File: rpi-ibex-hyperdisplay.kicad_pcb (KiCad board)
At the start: 2 copper layers, 99.1 x 113.5 mm, 66 parts, among them J1 Conn_02x05_Odd_Even, J2 USART_Connector_1, J3 Raspberry_Pi_2_3, J4 Hyperpixel_4.0_Touch, U1 ATmega328PB-AU, Y1 16MHz

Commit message: mirror flip the hyperpixel connector (oops :/)
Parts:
- 2/@ ('): renamed from 2/@ (`)
- 7/& (`): renamed from 7/& (')
- moved J3 12.5 mm to (135.6, 68.3), turned to 180 degrees
- moved J4 3.59 mm to (132.3, 66.8)
- renumbered 10K to R1, 1K to R2, 1K to R3
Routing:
- net BCM1: track 17.6 -> 160.1 mm, vias 0 -> 1
- net BCM0: track 11.4 -> 146.1 mm, vias 0 -> 1
- net BCM7: track 17.6 -> 147.9 mm, vias 0 -> 1
- net RPI_3.3V: track 213.0 -> 340.9 mm, vias 8 -> 12
- net BCM8: track 17.6 -> 139.2 mm, vias 0 -> 1
- net BCM25: track 17.6 -> 126.0 mm, vias 0 -> 1
- net BCM11: track 83.1 -> 187.2 mm, vias 2 -> 4
- net BCM9: track 11.4 -> 105.4 mm, vias 0 -> 1
- net BCM24: track 17.6 -> 105.6 mm, vias 0 -> 1
- net BCM23: track 17.6 -> 98.0 mm, vias 0 -> 1
- net BCM22: track 11.4 -> 91.5 mm, vias 0 -> 1
- net BCM10: track 82.1 -> 160.0 mm, vias 2 -> 4
- net BCM18: track 17.6 -> 91.4 mm, vias 0 -> 1
- net BCM27: track 11.4 -> 84.9 mm, vias 0 -> 1
- net BCM17: track 11.4 -> 81.0 mm, vias 0 -> 1
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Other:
- board text added: "Yovan Naumovski, 2019 rpi-ibex v0.4"
- board text removed: "Yovan Naumovski, 2019 rpi-ibex v0.3"

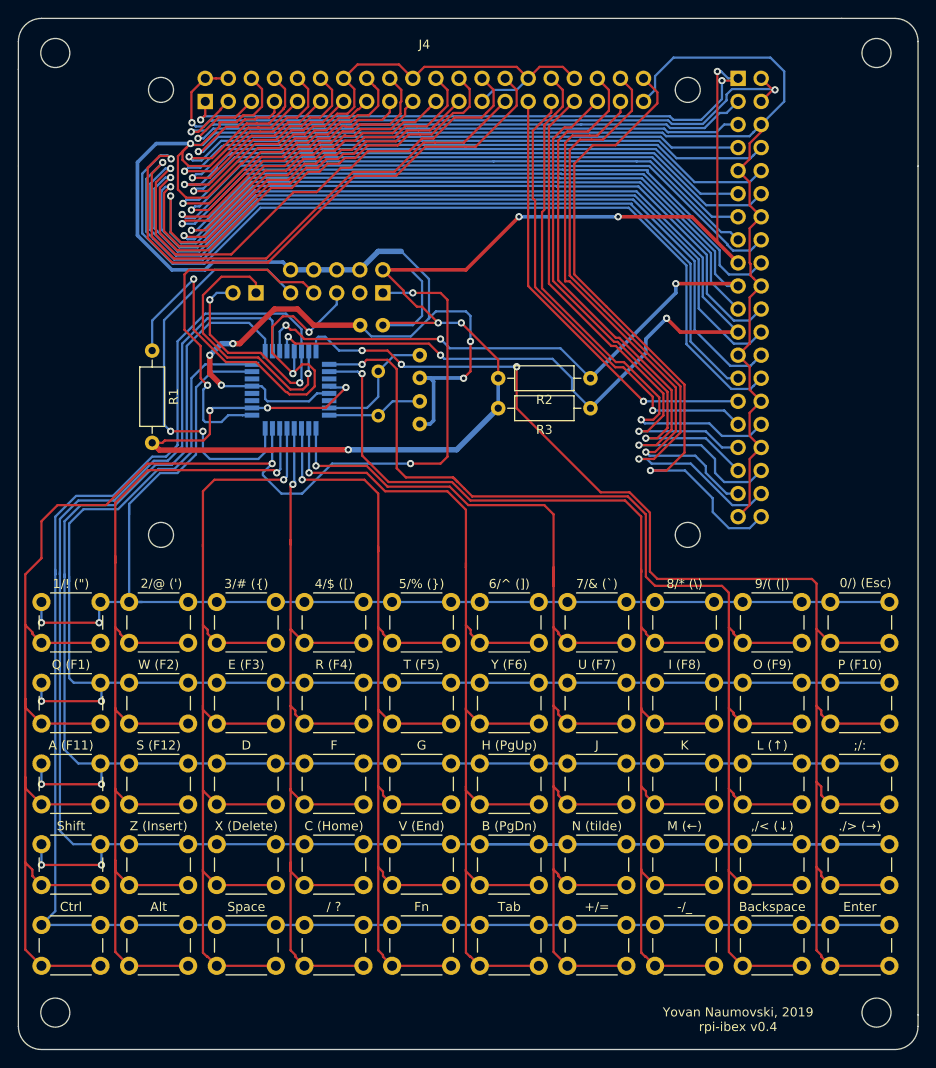
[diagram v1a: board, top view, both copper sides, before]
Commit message: move hyperpixel footprint silkscreen and other layers from back to front
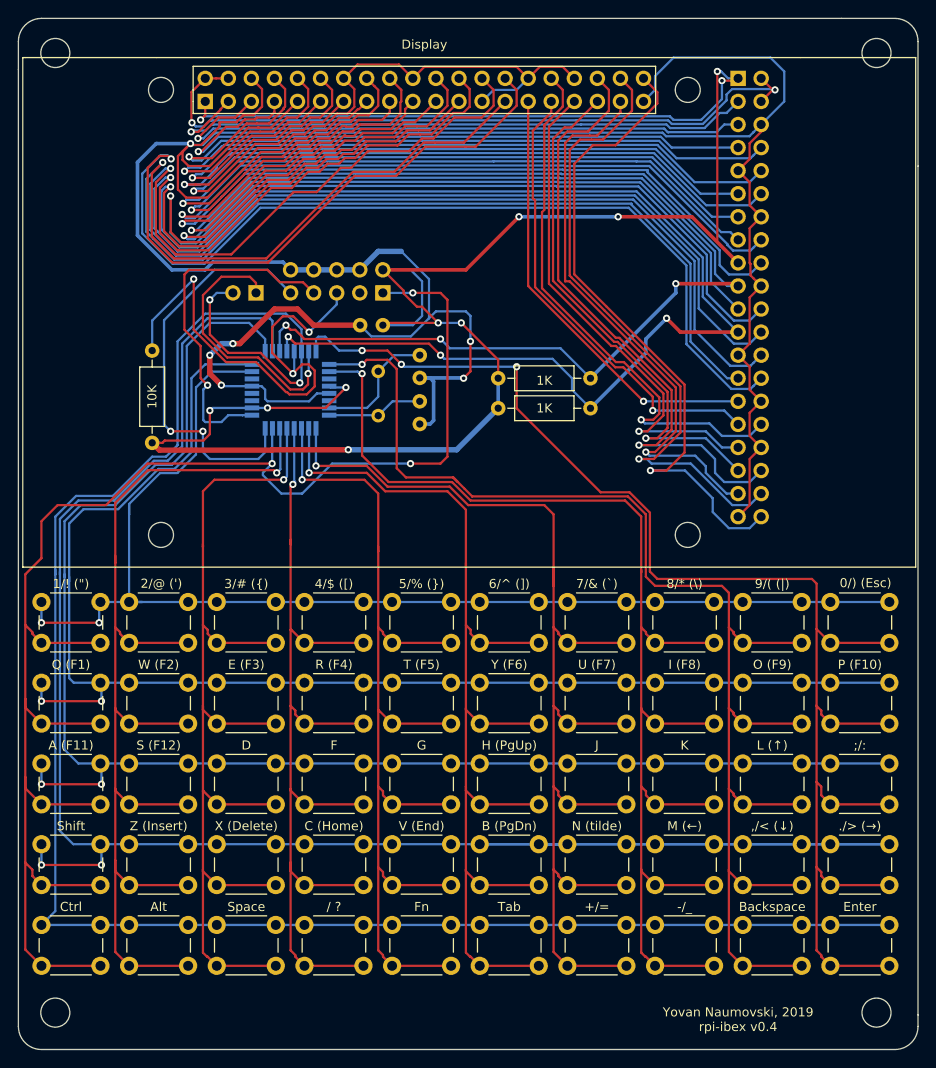
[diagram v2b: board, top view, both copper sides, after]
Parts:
- removed J4: Hyperpixel_4.0_Touch, TFT_modules:Hyperpixel_4.0_Touch
- added Display: Hyperpixel_4.0_Touch, TFT_modules:Hyperpixel_4.0_Touch, F.Cu at (132.3, 66.8)
- renumbered R1 to 10K, R2 to 1K, R3 to 1K
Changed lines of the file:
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@@
   (page A4)
   (layers
-    (0 F.Cu signal)
-    (31 B.Cu signal)
+    (0 F.Cu signal hide)
+    (31 B.Cu signal hide)
     (32 B.Adhes user)
-    (33 F.Adhes user)
+    (33 F.Adhes user hide)
     (34 B.Paste user)
     (35 F.Paste user)
@@
     (descr "Resistor, Axial_DIN0207 series, Axial, Horizontal, pin pitch=10.16mm, 0.25W = 1/4W, length*diameter=6.3*2.5mm^2, http://cdn-reichelt.de/documents/datenblatt/B400/1_4W%23YAG.pdf")
     (tags "Resistor Axial_DIN0207 series Axial Horizontal pin pitch 10.16mm 0.25W = 1/4W length 6.3mm diameter 2.5mm")
-    (fp_text reference R2 (at 5.08 -2.37) (layer F.SilkS)
+    (fp_text reference 1K (at 5.08 -0.254) (layer F.SilkS)
       (effects (font (size 1 1) (thickness 0.15)))
     )
@@
     (descr "Resistor, Axial_DIN0207 series, Axial, Horizontal, pin pitch=10.16mm, 0.25W = 1/4W, length*diameter=6.3*2.5mm^2, http://cdn-reichelt.de/documents/datenblatt/B400/1_4W%23YAG.pdf")
     (tags "Resistor Axial_DIN0207 series Axial Horizontal pin pitch 10.16mm 0.25W = 1/4W length 6.3mm diameter 2.5mm")
-    (fp_text reference R1 (at 5.08 -2.37 90) (layer F.SilkS)
+    (fp_text reference 10K (at 5.08 0 90) (layer F.SilkS)
       (effects (font (size 1 1) (thickness 0.15)))
     )
@@
     (descr "Resistor, Axial_DIN0207 series, Axial, Horizontal, pin pitch=10.16mm, 0.25W = 1/4W, length*diameter=6.3*2.5mm^2, http://cdn-reichelt.de/documents/datenblatt/B400/1_4W%23YAG.pdf")
     (tags "Resistor Axial_DIN0207 series Axial Horizontal pin pitch 10.16mm 0.25W = 1/4W length 6.3mm diameter 2.5mm")
-    (fp_text reference R3 (at 5.08 -2.37) (layer F.SilkS)
+    (fp_text reference 1K (at 5.08 0) (layer F.SilkS)
       (effects (font (size 1 1) (thickness 0.15)))
     )
@@
     (descr "Raspberry Pi Zero using through hole straight pin socket, 2x20, 2.54mm pitch, https://www.raspberrypi.org/documentation/hardware/raspberrypi/mechanical/rpi_MECH_Zero_1p2.pdf")
     (tags "raspberry pi zero through hole")
-    (fp_text reference J4 (at -2.206 31.242) (layer F.SilkS)
+    (fp_text reference Display (at -2.206 31.242) (layer F.SilkS)
       (effects (font (size 1 1) (thickness 0.15)))
     )
-    (fp_text value Hyperpixel_4.0_Touch (at 14.294 31.242) (layer B.Fab)
-      (effects (font (size 1 1) (thickness 0.15)) (justify mirror))
+    (fp_text value Hyperpixel_4.0_Touch (at 14.294 31.242) (layer F.Fab)
+      (effects (font (size 1 1) (thickness 0.15)))
     )
-    (fp_line (start -0.766 1.742) (end -0.766 60.742) (layer B.SilkS) (width 0.12))
-    (fp_line (start 5.334 55.642) (end 5.334 5.842) (layer B.Fab) (width 0.1))
-    (fp_line (start 0.254 56.642) (end 4.334 56.642) (layer B.Fab) (width 0.1))
-    (fp_line (start 4.334 56.642) (end 5.334 55.642) (layer B.Fab) (width 0.1))
-    (fp_line (start 0.194 5.782) (end 5.394 5.782) (layer B.SilkS) (width 0.12))
-    (fp_line (start 5.394 54.102) (end 5.394 5.782) (layer B.SilkS) (width 0.12))
-    (fp_line (start 5.394 56.702) (end 5.394 55.372) (layer B.SilkS) (width 0.12))
-    (fp_line (start 4.064 56.702) (end 5.394 56.702) (layer B.SilkS) (width 0.12))
-    (fp_line (start 2.794 54.102) (end 5.394 54.102) (layer B.SilkS) (width 0.12))
-    (fp_line (start 2.794 56.702) (end 2.794 54.102) (layer B.SilkS) (width 0.12))
-    (fp_line (start 5.824 5.372) (end -0.276 5.372) (layer B.CrtYd) (width 0.05))
-    (fp_line (start -0.276 5.372) (end -0.276 57.172) (layer B.CrtYd) (width 0.05))
-    (fp_line (start -0.276 57.172) (end 5.824 57.172) (layer B.CrtYd) (width 0.05))
-    (fp_line (start 5.824 57.172) (end 5.824 5.372) (layer B.CrtYd) (width 0.05))
-    (fp_line (start 0.194 56.702) (end 2.794 56.702) (layer B.SilkS) (width 0.12))
-    (fp_line (start 0.194 56.702) (end 0.194 5.782) (layer B.SilkS) (width 0.12))
-    (fp_line (start 5.334 5.842) (end 0.254 5.842) (layer B.Fab) (width 0.1))
-    (fp_line (start 0.254 5.842) (end 0.254 56.642) (layer B.Fab) (width 0.1))
-    (fp_text user %R (at 2.794 31.242 180) (layer B.Fab)
-      (effects (font (size 1 1) (thickness 0.15)) (justify mirror))
-    )
-    (fp_line (start -0.706 1.742) (end -0.706 60.742) (layer B.Fab) (width 0.1))
-    (fp_line (start -0.766 60.742) (end -0.766 68.616) (layer B.SilkS) (width 0.12))
-    (fp_line (start -0.766 68.616) (end -0.766 75.184) (layer B.SilkS) (width 0.12))
-    (fp_line (start -0.766 75.184) (end -0.766 75.438) (layer B.SilkS) (width 0.12))
-    (fp_line (start -0.766 1.742) (end -0.766 -10.196) (layer B.SilkS) (width 0.12))
-    (fp_line (start -0.766 -10.196) (end -0.766 -22.86) (layer B.SilkS) (width 0.12))
-    (fp_line (start -0.706 60.742) (end -0.706 75.22) (layer B.Fab) (width 0.12))
-    (fp_line (start -0.706 75.22) (end -0.706 75.4232) (layer B.Fab) (width 0.12))
-    (fp_line (start 55.3264 60.1578) (end 55.3264 71.537) (layer B.Fab) (width 0.12))
-    (fp_line (start -0.706 75.4232) (end 55.0978 75.4232) (layer B.Fab) (width 0.12))
-    (fp_line (start 55.3264 71.537) (end 55.3264 75.3978) (layer B.Fab) (width 0.12))
-    (fp_line (start 55.0978 75.4232) (end 55.301 75.4232) (layer B.Fab) (width 0.12))
-    (fp_line (start 55.301 75.4232) (end 55.3264 75.4232) (layer B.Fab) (width 0.12))
-    (fp_line (start -0.706 1.742) (end -0.706 -22.8494) (layer B.Fab) (width 0.12))
-    (fp_line (start -0.706 -22.8494) (end 54.2342 -22.8494) (layer B.Fab) (width 0.12))
-    (fp_line (start 55.3264 60.1578) (end 55.3264 -22.8494) (layer B.Fab) (width 0.12))
-    (fp_line (start 54.2342 -22.8494) (end 55.3264 -22.8494) (layer B.Fab) (width 0.12))
-    (fp_line (start -0.766 -22.86) (end 55.3426 -22.86) (layer B.SilkS) (width 0.12))
-    (fp_line (start 55.3426 -22.86) (end 55.3426 75.4634) (layer B.SilkS) (width 0.12))
-    (fp_line (start 55.3426 75.4634) (end -0.766 75.4634) (layer B.SilkS) (width 0.12))
+    (fp_line (start -0.766 1.742) (end -0.766 60.742) (layer F.SilkS) (width 0.12))
+    (fp_line (start 5.334 55.642) (end 5.334 5.842) (layer F.Fab) (width 0.1))
+    (fp_line (start 0.254 56.642) (end 4.334 56.642) (layer F.Fab) (width 0.1))
+    (fp_line (start 5.334 56.642) (end 5.334 55.642) (layer F.Fab) (width 0.1))
+    (fp_line (start 0.194 5.782) (end 5.394 5.782) (layer F.SilkS) (width 0.12))
+    (fp_line (start 5.394 54.102) (end 5.394 5.782) (layer F.SilkS) (width 0.12))
+    (fp_line (start 5.394 56.702) (end 5.394 55.372) (layer F.SilkS) (width 0.12))
+    (fp_line (start 4.064 56.702) (end 5.394 56.702) (layer F.SilkS) (width 0.12))
+    (fp_line (start 5.394 55.372) (end 5.394 54.102) (layer F.SilkS) (width 0.12))
+    (fp_line (start 2.794 56.702) (end 4.064 56.702) (layer F.SilkS) (width 0.12))
+    (fp_line (start 5.824 5.372) (end -0.276 5.372) (layer F.CrtYd) (width 0.05))
+    (fp_line (start -0.276 5.372) (end -0.276 57.172) (layer F.CrtYd) (width 0.05))
+    (fp_line (start -0.276 57.172) (end 5.824 57.172) (layer F.CrtYd) (width 0.05))
+    (fp_line (start 5.824 57.172) (end 5.824 5.372) (layer F.CrtYd) (width 0.05))
+    (fp_line (start 0.194 56.702) (end 2.794 56.702) (layer F.SilkS) (width 0.12))
+    (fp_line (start 0.194 56.702) (end 0.194 5.782) (layer F.SilkS) (width 0.12))
+    (fp_line (start 5.334 5.842) (end 0.254 5.842) (layer F.Fab) (width 0.1))
+    (fp_line (start 0.254 5.842) (end 0.254 56.642) (layer F.Fab) (width 0.1))
+    (fp_text user %R (at 2.794 31.242 180) (layer F.Fab)
+      (effects (font (size 1 1) (thickness 0.15)) (justify mirror))
+    )
+    (fp_line (start -0.706 1.742) (end -0.706 60.742) (layer F.Fab) (width 0.1))
+    (fp_line (start -0.766 60.742) (end -0.766 68.616) (layer F.SilkS) (width 0.12))
+    (fp_line (start -0.766 68.616) (end -0.766 75.184) (layer F.SilkS) (width 0.12))
+    (fp_line (start -0.766 75.184) (end -0.766 75.438) (layer F.SilkS) (width 0.12))
+    (fp_line (start -0.766 1.742) (end -0.766 -10.196) (layer F.SilkS) (width 0.12))
+    (fp_line (start -0.766 -10.196) (end -0.766 -22.86) (layer F.SilkS) (width 0.12))
+    (fp_line (start -0.706 60.742) (end -0.706 75.22) (layer F.Fab) (width 0.12))
+    (fp_line (start -0.706 75.22) (end -0.706 75.4232) (layer F.Fab) (width 0.12))
+    (fp_line (start 55.3264 60.1578) (end 55.3264 71.537) (layer F.Fab) (width 0.12))
+    (fp_line (start -0.706 75.4232) (end 55.0978 75.4232) (layer F.Fab) (width 0.12))
+    (fp_line (start 55.3264 71.537) (end 55.3264 75.3978) (layer F.Fab) (width 0.12))
+    (fp_line (start 55.0978 75.4232) (end 55.301 75.4232) (layer F.Fab) (width 0.12))
+    (fp_line (start 55.301 75.4232) (end 55.3264 75.4232) (layer F.Fab) (width 0.12))
+    (fp_line (start -0.706 1.742) (end -0.706 -22.8494) (layer F.Fab) (width 0.12))
+    (fp_line (start -0.706 -22.8494) (end 54.2342 -22.8494) (layer F.Fab) (width 0.12))
+    (fp_line (start 55.3264 60.1578) (end 55.3264 -22.8494) (layer F.Fab) (width 0.12))
+    (fp_line (start 54.2342 -22.8494) (end 55.3264 -22.8494) (layer F.Fab) (width 0.12))
+    (fp_line (start -0.766 -22.86) (end 55.3426 -22.86) (layer F.SilkS) (width 0.12))
+    (fp_line (start 55.3426 -22.86) (end 55.3426 75.4634) (layer F.SilkS) (width 0.12))
+    (fp_line (start 55.3426 75.4634) (end -0.766 75.4634) (layer F.SilkS) (width 0.12))
     (fp_line (start -0.766 75.4634) (end -0.766 75.438) (layer B.SilkS) (width 0.12))
+    (fp_line (start 4.334 56.642) (end 5.334 56.642) (layer F.Fab) (width 0.1))
     (pad 6 thru_hole oval (at 1.524 50.292 270) (size 1.7 1.7) (drill 1) (layers *.Cu *.Mask)
       (net 1 GND))

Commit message: rotate the rpi pin headers so that its usb ports are facing outwards the board
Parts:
- moved J3 50.1 mm to (137.9, 118.4), turned to 0 degrees
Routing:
- net RPI_3.3V: track 340.9 -> 562.1 mm, vias 12 -> 13
- net BCM5: track 48.7 -> 166.8 mm, vias 1 -> 2
- net BCM10: track 160.0 -> 241.8 mm
- net BCM11: track 187.2 -> 264.4 mm
- net BCM21: track 72.9 -> 14.1 mm, vias 1 -> 0
- net GND: track 369.5 -> 427.8 mm, vias 6 -> 12
- net BCM20: track 70.8 -> 21.3 mm, vias 1 -> 2
- net BCM16: track 69.1 -> 21.7 mm, vias 1 -> 0
- net BCM3: track 68.0 -> 112.8 mm, vias 1 -> 2
- net BCM2: track 67.5 -> 110.4 mm, vias 1 -> 2
- net BCM4: track 72.0 -> 112.5 mm, vias 1 -> 2
- net BCM26: track 62.5 -> 22.6 mm, vias 1 -> 0
- net BCM12: track 61.0 -> 26.6 mm, vias 1 -> 0
- net BCM17: track 81.0 -> 114.2 mm, vias 1 -> 2
- net BCM13: track 56.3 -> 23.2 mm, vias 1 -> 0
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
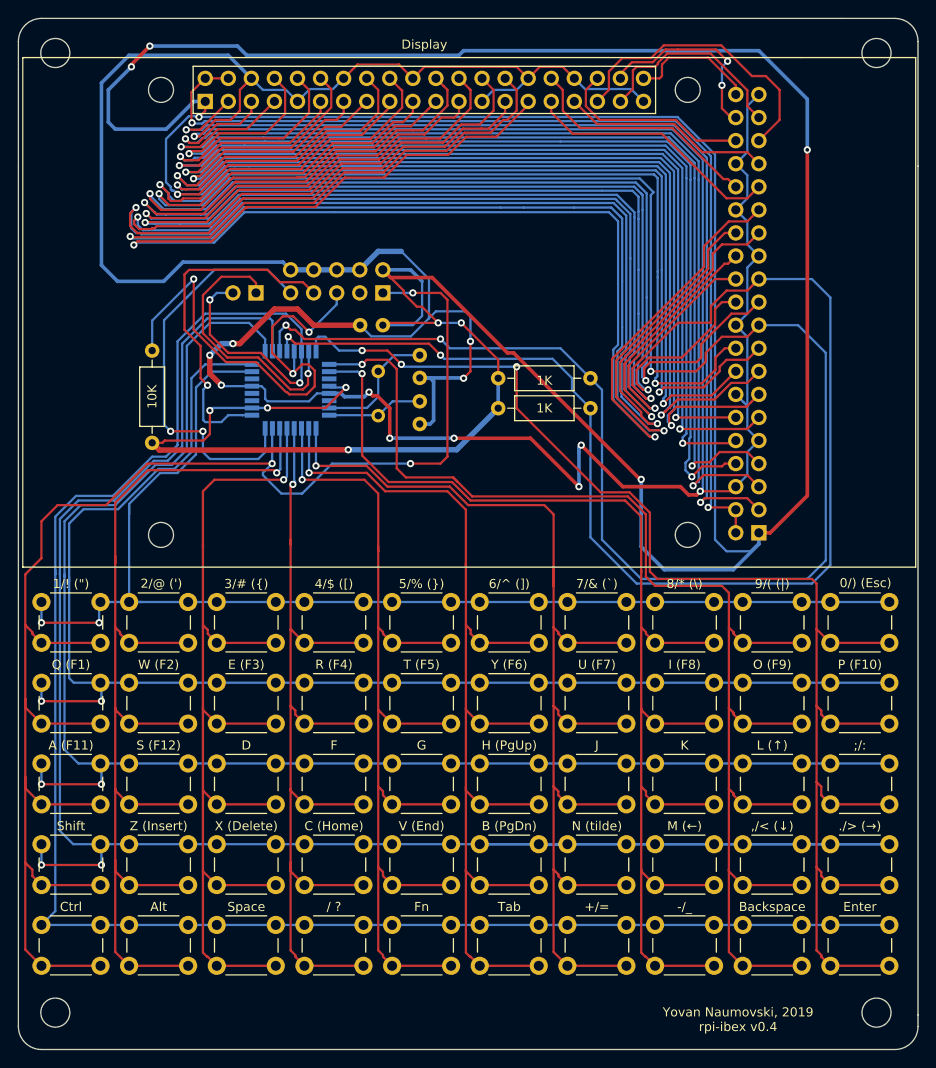
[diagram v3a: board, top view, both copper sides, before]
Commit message: better route tracks layout for the connection between the raspberry pi and hyperpixel display
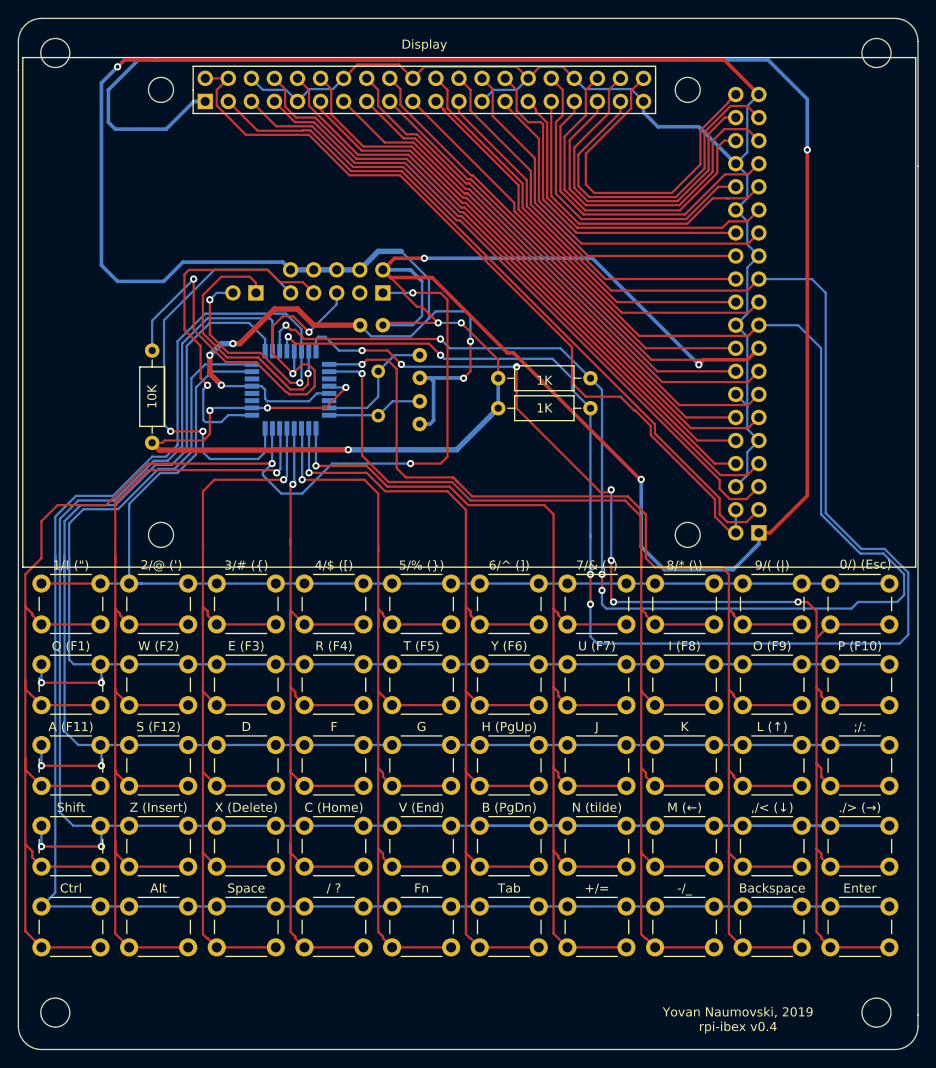
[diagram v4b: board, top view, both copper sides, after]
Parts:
- moved +/= 2.03 mm to (116.8, 159.5)
- moved -/_ 2.03 mm to (126.5, 159.5)
- moved / ? 2.03 mm to (87.9, 159.5)
- moved ;/: 2.03 mm to (145.8, 141.7)
- moved A (F11) 2.03 mm to (58.9, 141.7)
- moved Alt 2.03 mm to (68.6, 159.5)
- moved Backspace 2.03 mm to (136.1, 159.5)
- moved Ctrl 2.03 mm to (58.9, 159.5)
- moved D 2.03 mm to (78.2, 141.7)
- moved Enter 2.03 mm to (145.8, 159.5)
- moved F 2.03 mm to (87.9, 141.7)
- moved Fn 2.03 mm to (97.5, 159.5)
- moved G 2.03 mm to (97.5, 141.7)
- moved H (PgUp) 2.03 mm to (107.2, 141.7)
- moved J 2.03 mm to (116.8, 141.7)
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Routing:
- net RPI_3.3V: track 562.1 -> 416.2 mm, vias 13 -> 10
- net BCM5: track 166.8 -> 37.3 mm, vias 2 -> 0
- net BCM1: track 166.3 -> 38.6 mm, vias 2 -> 0
- net BCM0: track 166.5 -> 39.2 mm, vias 2 -> 0
- net BCM7: track 155.7 -> 40.7 mm, vias 2 -> 0
- net BCM8: track 146.2 -> 43.1 mm, vias 2 -> 0
- net BCM25: track 139.7 -> 46.0 mm, vias 2 -> 0
- net GND: track 427.8 -> 335.3 mm, vias 12 -> 6
- net BCM9: track 133.7 -> 47.3 mm, vias 2 -> 0
- net BCM24: track 126.9 -> 51.4 mm, vias 2 -> 0
- net BCM11: track 264.4 -> 195.5 mm
- net BCM23: track 120.3 -> 55.0 mm, vias 2 -> 0
- net BCM22: track 121.2 -> 56.5 mm, vias 2 -> 0
- net BCM27: track 115.9 -> 60.1 mm, vias 2 -> 0
- net BCM10: track 241.8 -> 188.8 mm
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
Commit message: improve layout
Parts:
- moved 0/) (Esc) 1.78 mm to (145.8, 125.7)
- moved 1/! (") 1.78 mm to (58.9, 125.7)
- moved 2/@ (') 1.78 mm to (68.6, 125.7)
- moved 3/# ({) 1.78 mm to (78.2, 125.7)
- moved 4/$ ([) 1.78 mm to (87.9, 125.7)
- moved 5/% (}) 1.78 mm to (97.5, 125.7)
- moved 6/^ (]) 1.78 mm to (107.2, 125.7)
- moved 7/& (`) 1.78 mm to (116.8, 125.7)
- moved 8/* (\) 1.78 mm to (126.5, 125.7)
- moved 9/( (|) 1.78 mm to (136.1, 125.7)
- moved +/= 1.78 mm to (116.8, 161.3)
- moved ,/< (↓) 1.78 mm to (136.1, 152.4)
- moved -/_ 1.78 mm to (126.5, 161.3)
- moved ./> (→) 1.78 mm to (145.8, 152.4)
- moved / ? 1.78 mm to (87.9, 161.3)
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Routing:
- net BCM11: track 195.5 -> 199.2 mm
- net BCM10: track 188.8 -> 192.3 mm
- net KB_COL_7: track 123.2 -> 125.5 mm
- net KB_COL_8: track 138.2 -> 140.5 mm
- net KB_ROW_2: track 150.9 -> 153.0 mm
- net KB_COL_6: track 117.6 -> 119.7 mm
- net KB_ROW_4: track 228.7 -> 230.4 mm
- net KB_ROW_3: track 168.0 -> 169.8 mm
- net KB_COL_1: track 175.1 -> 176.9 mm
- net KB_ROW_5: track 207.0 -> 208.8 mm
- net KB_ROW_1: track 127.9 -> 129.7 mm
- net KB_COL_10: track 159.7 -> 161.4 mm
- net KB_COL_9: track 147.3 -> 148.7 mm
